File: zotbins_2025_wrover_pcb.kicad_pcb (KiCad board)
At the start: 2 copper layers, 26 parts, among them J1 FFC2B28-24-G, J5 DCJ200-10-A-XX-K_REVA, J6 Conn_01x30_Pin, U1 ESP32-WROVER-E/IE-DEVKIT-C, U2 MCP23017_SP, U3 XC6206P122MR-G, U4 XC6206P282PR-G, U5 LM7805_TO220

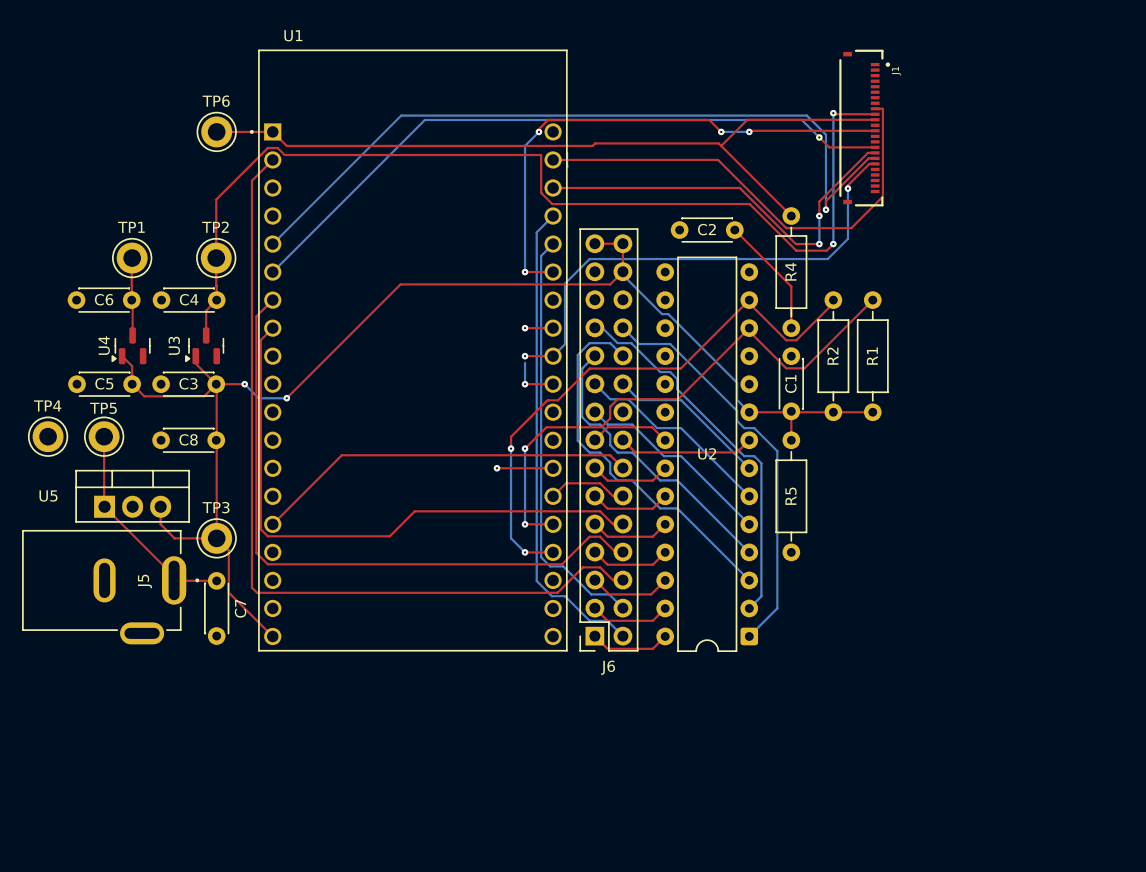
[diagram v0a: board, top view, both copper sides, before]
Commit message: resolved ERC checks, footprint incompatibilities, symbol library not found errors; 3 ERC violations surpressed intentionally
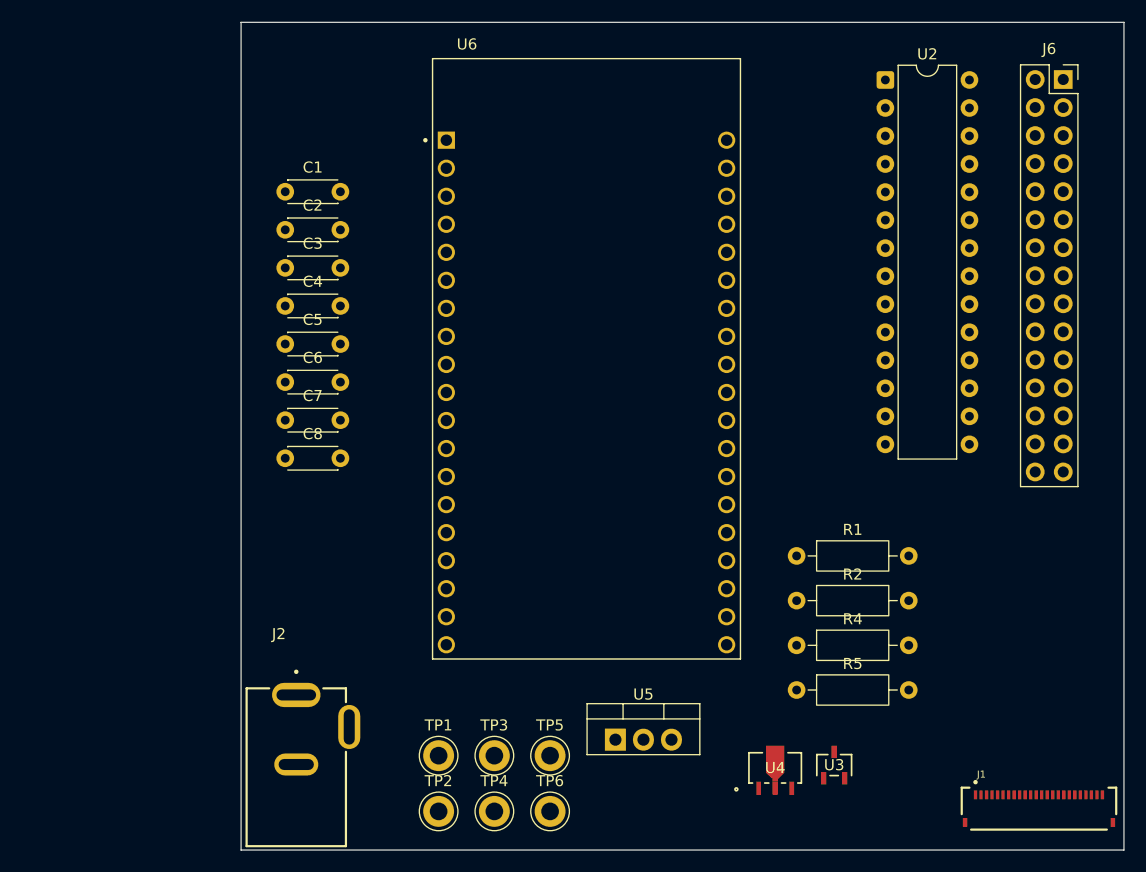
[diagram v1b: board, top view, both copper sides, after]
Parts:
- removed J5: DCJ200-10-A-XX-K_REVA, Connector_BarrelJack:GCT_DCJ200-10-A-XX-K_REVA
- removed U1: ESP32-WROVER-E/IE-DEVKIT-C, MCU_Development_Board:MODULE_ESP32-DEVKITC-32D
- added J2: DCJ200-10-A-XX-K_REVA, Library:GCT_DCJ200-10-A-XX-K_REVA, F.Cu at (105.0, 132.5)
- added U6: ESP32-DEVKITC-32D, ESP32-DEVKITC-32D:MODULE_ESP32-DEVKITC-32D, F.Cu at (131.3, 95.4)
- J1: footprint Connector_FFC-FPC:GCT_FFC2B28-24-G -> Library:GCT_FFC2B28-24-G
- U3: value XC6206P122MR-G -> XC6206P302MR-G; footprint Package_TO_SOT_SMD:SOT-23 -> XC6206P302MR_G:SOT-23_TOR
- U4: footprint Package_TO_SOT_SMD:SOT-23 -> XC6206P282PR_G:SOT-89_TOR
- moved U4 69.7 mm to (148.4, 132.6), turned to 0 degrees
- moved TP6 68.6 mm to (128.0, 136.5)
- moved U3 68.4 mm to (153.7, 132.3), turned to 0 degrees
- moved J6 65.9 mm to (174.5, 70.2), turned to 0 degrees
- moved J1 63.7 mm to (172.3, 136.2), turned to 0 degrees
- moved TP2 54.0 mm to (117.9, 136.5)
- moved TP1 53.0 mm to (117.9, 131.4)
- moved TP4 52.8 mm to (123.0, 136.5)
- moved U2 51.9 mm to (158.4, 70.2), turned to 0 degrees
- moved U5 50.9 mm to (133.9, 130.0)
- moved C1 50.0 mm to (104.0, 80.3), turned to 0 degrees
- moved TP5 49.7 mm to (128.0, 131.4)
- moved C2 40.7 mm to (104.0, 83.8), turned to 0 degrees
- moved R4 38.9 mm to (150.3, 121.5), turned to 0 degrees
- moved TP3 31.9 mm to (123.0, 131.4)
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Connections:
- U3 pad 1: +5V -> GND
- U3 pad 2: GND -> CSI_1V2
- U3 pad 3: CSI_1V2 -> +5V
- U4 pad 1: +5V -> GND
- U4 pad 2: GND -> +5V
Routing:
- net +5V: track 125.1 -> 0.00 mm, vias 2 -> 0
- net CSI_1V2: track 92.4 -> 0.00 mm, vias 2 -> 0
- net /EN: track 74.8 -> 0.00 mm
- net +3V3: track 70.3 -> 0.00 mm
- net /DATA6: track 69.3 -> 0.00 mm, vias 1 -> 0
- net /DATA7: track 61.3 -> 0.00 mm, vias 1 -> 0
- net /GPIO32: track 58.8 -> 0.00 mm
- net /GPIO33: track 53.2 -> 0.00 mm
- net /GPIO_SCK: track 51.2 -> 0.00 mm, vias 2 -> 0
- net /GPIO_SDA: track 50.3 -> 0.00 mm, vias 2 -> 0
- net /XCLK1: track 47.3 -> 0.00 mm, vias 4 -> 0
- net /DATA2: track 45.0 -> 0.00 mm, vias 2 -> 0
- net /TX: track 43.6 -> 0.00 mm
- net /HREF: track 42.3 -> 0.00 mm
- net /PCLK: track 38.3 -> 0.00 mm, vias 2 -> 0
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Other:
- board outline added: 80 x 75 mm

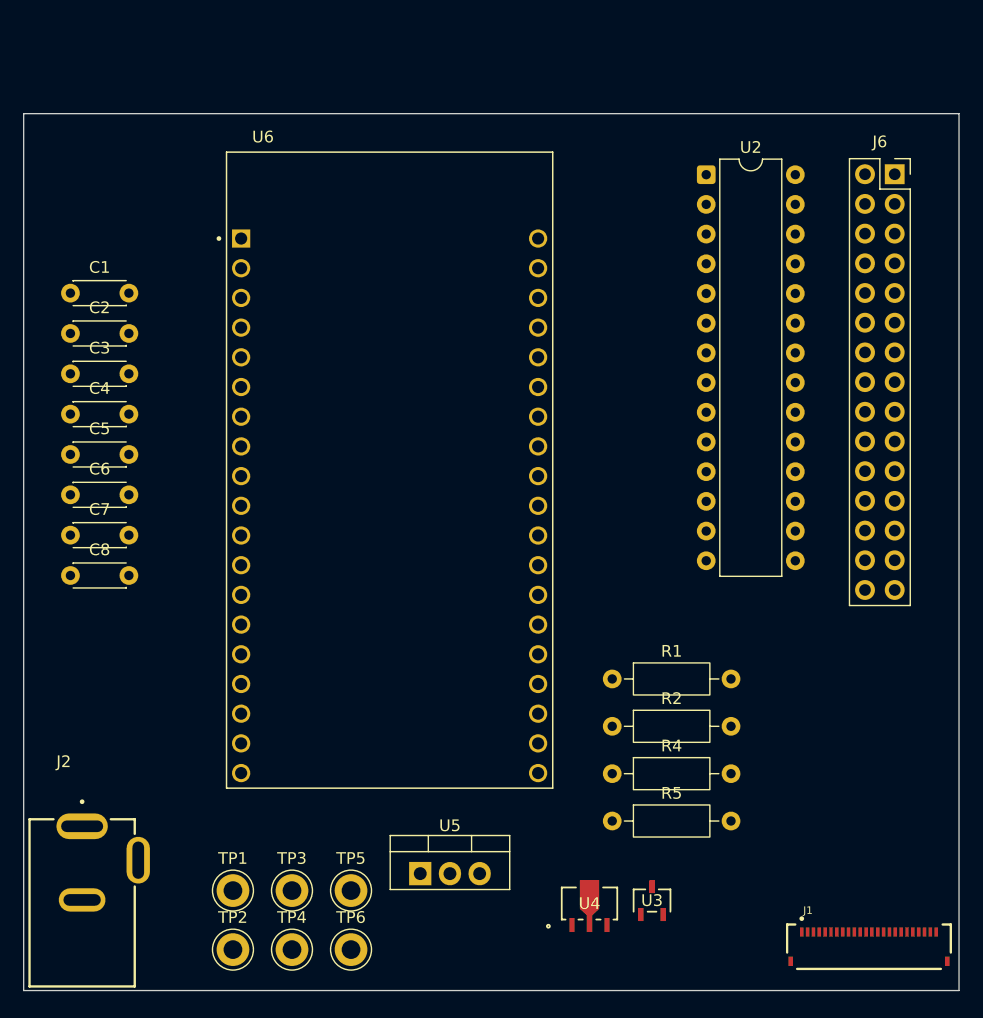
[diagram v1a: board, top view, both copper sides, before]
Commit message: configured power section ratsnest
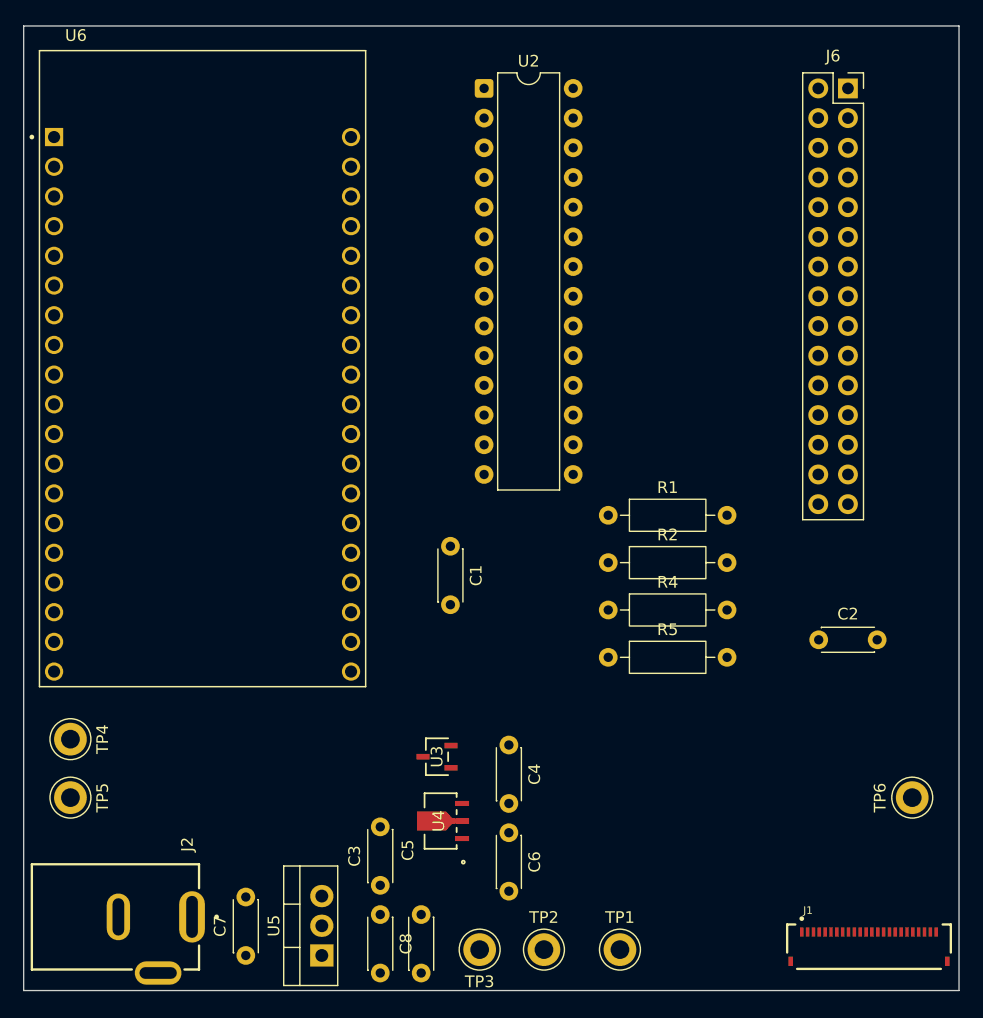
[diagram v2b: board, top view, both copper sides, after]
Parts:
- J2: value DCJ200-10-A-XX-K_REVA -> Barrel Jack
- TP1: value TestPoint -> CSI_2V8
- TP2: value TestPoint -> CSI_1V2
- TP3: value TestPoint -> RegVo
- TP4: value TestPoint -> GND
- TP5: value TestPoint -> Vin
- TP6: value TestPoint -> DOVDD
- moved C2 69.2 mm to (168.0, 110.0)
- moved C3 51.1 mm to (130.5, 131.0), turned to 90 degrees
- moved TP6 49.7 mm to (176.0, 123.5), turned to 90 degrees
- moved C5 49.5 mm to (134.0, 133.5), turned to -90 degrees
- moved C6 47.3 mm to (141.5, 126.5), turned to -90 degrees
- moved C4 47.0 mm to (141.5, 119.0), turned to -90 degrees
- moved C8 39.3 mm to (130.5, 133.5), turned to -90 degrees
- moved C1 39.1 mm to (136.5, 102.0), turned to -90 degrees
- moved C7 39.0 mm to (119.0, 137.0), turned to 90 degrees
- moved TP1 33.5 mm to (151.0, 136.5)
- moved TP2 26.6 mm to (144.5, 136.5)
- moved TP4 26.1 mm to (104.0, 118.5), turned to -90 degrees
- moved TP5 25.3 mm to (104.0, 123.5), turned to -90 degrees
- moved U3 22.1 mm to (135.4, 120.0), turned to 90 degrees
- moved U2 20.4 mm to (139.4, 62.8)
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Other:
- board size 80 x 75 mm -> 80 x 82.5 mm

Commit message: sorted ratsnest
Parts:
- moved R5 24.8 mm to (158.9, 88.4), turned to -90 degrees
- moved R2 23.1 mm to (138.4, 83.4), turned to -90 degrees
- moved R1 22.2 mm to (134.5, 83.4), turned to -90 degrees
- moved R4 22.2 mm to (150.4, 129.7)
- moved TP6 21.8 mm to (158.3, 136.3), turned to 0 degrees
- moved C1 19.6 mm to (142.8, 83.4)
- moved C2 16.5 mm to (160.5, 124.7), turned to 180 degrees
- moved U2 7.50 mm to (146.9, 63.1)
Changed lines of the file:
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@@
 	(footprint "TestPoint:TestPoint_Keystone_5005-5009_Compact"
 		(layer "F.Cu")
-		(at 176 123.5 90)
+		(at 158.35 136.325)
 		(descr "Keystone THM Compact Test Point 5005-5009, http://www.keyelco.com/product-pdf.cfm?p=1314")
 		(tags "Through Hole Mount Test Points")
 		(property "Reference" "TP6"
-			(at 0 -2.75 90)
+			(at 0 -2.75 0)
 			(layer "F.SilkS")
 			(effects
@@
 		)
 		(property "Value" "DOVDD"
-			(at 0 2.75 90)
+			(at 0 2.75 0)
 			(layer "F.Fab")
 			(effects
@@
 		)
 		(property "Datasheet" "~"
-			(at 0 0 90)
+			(at 0 0 0)
 			(unlocked yes)
 			(layer "F.Fab")
@@
 		)
 		(property "Description" "test point"
-			(at 0 0 90)
+			(at 0 0 0)
 			(unlocked yes)
 			(layer "F.Fab")
@@
 		)
 		(fp_text user "${REFERENCE}"
-			(at 0 0 90)
+			(at 0 0 0)
 			(layer "F.Fab")
 			(effects
@@
 		)
 		(pad "1" thru_hole circle
-			(at 0 0 90)
+			(at 0 0)
 			(size 2.8 2.8)
 			(drill 1.6)
@@
 	(footprint "Capacitor_THT:C_Disc_D4.3mm_W1.9mm_P5.00mm"
 		(layer "F.Cu")
-		(at 136.5 102 -90)
+		(at 142.775 83.4 -90)
 		(descr "C, Disc series, Radial, pin pitch=5.00mm, diameter*width=4.3*1.9mm^2, Capacitor, http://www.vishay.com/docs/45233/krseries.pdf")
 		(tags "C Disc series Radial pin pitch 5.00mm diameter 4.3mm width 1.9mm Capacitor")
@@
 	(footprint "Resistor_THT:R_Axial_DIN0207_L6.3mm_D2.5mm_P10.16mm_Horizontal"
 		(layer "F.Cu")
-		(at 150 99.35)
+		(at 134.5 83.415 -90)
 		(descr "Resistor, Axial_DIN0207 series, Axial, Horizontal, pin pitch=10.16mm, 0.25W = 1/4W, length*diameter=6.3*2.5mm^2, http://cdn-reichelt.de/documents/datenblatt/B400/1_4W%23YAG.pdf")
 		(tags "Resistor Axial_DIN0207 series Axial Horizontal pin pitch 10.16mm 0.25W = 1/4W length 6.3mm diameter 2.5mm")
 		(property "Reference" "R1"
-			(at 5.08 -2.37 0)
+			(at 5.08 -2.37 90)
 			(layer "F.SilkS")
 			(effects
@@
 		)
 		(property "Value" "10k"
-			(at 5.08 2.37 0)
+			(at 5.08 2.37 90)
 			(layer "F.Fab")
 			(effects
@@
 		)
 		(property "Datasheet" "~"
-			(at 0 0 0)
+			(at 0 0 90)
 			(layer "F.Fab")
 			(hide yes)
@@
 		)
 		(property "Description" "Resistor, small symbol"
-			(at 0 0 0)
+			(at 0 0 90)
 			(layer "F.Fab")
 			(hide yes)
@@
 		)
 		(fp_text user "${REFERENCE}"
-			(at 5.08 0 0)
+			(at 5.08 0 90)
 			(layer "F.Fab")
 			(effects
@@
 		)
 		(pad "1" thru_hole circle
-			(at 0 0)
+			(at 0 0 270)
 			(size 1.6 1.6)
 			(drill 0.8)
@@
 		)
 		(pad "2" thru_hole circle
-			(at 10.16 0)
+			(at 10.16 0 270)
 			(size 1.6 1.6)
 			(drill 0.8)
@@
 	(footprint "Capacitor_THT:C_Disc_D4.3mm_W1.9mm_P5.00mm"
 		(layer "F.Cu")
-		(at 168 110)
+		(at 160.475 124.725 180)
 		(descr "C, Disc series, Radial, pin pitch=5.00mm, diameter*width=4.3*1.9mm^2, Capacitor, http://www.vishay.com/docs/45233/krseries.pdf")
 		(tags "C Disc series Radial pin pitch 5.00mm diameter 4.3mm width 1.9mm Capacitor")
@@
 		(attr through_hole)
 		(fp_line
-			(start 0.23 -1.07)
-			(end 4.77 -1.07)
+			(start 4.77 1.07)
+			(end 0.23 1.07)
 			(stroke
 				(width 0.12)
@@
 		)
 		(fp_line
-			(start 0.23 -1.014)
-			(end 0.23 -1.07)
+			(start 4.77 1.014)
+			(end 4.77 1.07)
 			(stroke
 				(width 0.12)
@@
 		)
 		(fp_line
-			(start 4.77 1.014)
-			(end 4.77 1.07)
+			(start 0.23 -1.014)
+			(end 0.23 -1.07)
 			(stroke
 				(width 0.12)
@@
 		)
 		(fp_line
-			(start 4.77 1.07)
-			(end 0.23 1.07)
+			(start 0.23 -1.07)
+			(end 4.77 -1.07)
 			(stroke
 				(width 0.12)
@@
 		)
 		(pad "1" thru_hole circle
-			(at 0 0)
+			(at 0 0 180)
 			(size 1.6 1.6)
 			(drill 0.8)
@@
 		)
 		(pad "2" thru_hole circle
-			(at 5 0)
+			(at 5 0 180)
 			(size 1.6 1.6)
 			(drill 0.8)
@@
 	(footprint "Package_DIP:DIP-28_W7.62mm"
 		(layer "F.Cu")
-		(at 139.38 62.84)
+		(at 146.88 63.06)
 		(descr "28-lead though-hole mounted DIP package, row spacing 7.62mm (300 mils)")
 		(tags "THT DIP DIL PDIP 2.54mm 7.62mm 300mil")
@@
 	(footprint "Resistor_THT:R_Axial_DIN0207_L6.3mm_D2.5mm_P10.16mm_Horizontal"
 		(layer "F.Cu")
-		(at 150 107.45)
+		(at 150.365 129.675)
 		(descr "Resistor, Axial_DIN0207 series, Axial, Horizontal, pin pitch=10.16mm, 0.25W = 1/4W, length*diameter=6.3*2.5mm^2, http://cdn-reichelt.de/documents/datenblatt/B400/1_4W%23YAG.pdf")
 		(tags "Resistor Axial_DIN0207 series Axial Horizontal pin pitch 10.16mm 0.25W = 1/4W length 6.3mm diameter 2.5mm")
@@
 	(footprint "Resistor_THT:R_Axial_DIN0207_L6.3mm_D2.5mm_P10.16mm_Horizontal"
 		(layer "F.Cu")
-		(at 150 111.5)
+		(at 158.925 88.415 -90)
 		(descr "Resistor, Axial_DIN0207 series, Axial, Horizontal, pin pitch=10.16mm, 0.25W = 1/4W, length*diameter=6.3*2.5mm^2, http://cdn-reichelt.de/documents/datenblatt/B400/1_4W%23YAG.pdf")
 		(tags "Resistor Axial_DIN0207 series Axial Horizontal pin pitch 10.16mm 0.25W = 1/4W length 6.3mm diameter 2.5mm")
 		(property "Reference" "R5"
-			(at 5.08 -2.37 0)
+			(at 5.08 -2.37 90)
 			(layer "F.SilkS")
 			(effects
@@
 		)
 		(property "Value" "10k"
-			(at 5.08 2.37 0)
+			(at 5.08 2.37 90)
 			(layer "F.Fab")
 			(effects
@@
 		)
 		(property "Datasheet" "~"
-			(at 0 0 0)
+			(at 0 0 90)
 			(layer "F.Fab")
 			(hide yes)
@@
 		)
 		(property "Description" "Resistor, small symbol"
-			(at 0 0 0)
+			(at 0 0 90)
 			(layer "F.Fab")
 			(hide yes)
@@
 		)
 		(fp_text user "${REFERENCE}"
-			(at 5.08 0 0)
+			(at 5.08 0 90)
 			(layer "F.Fab")
 			(effects
@@
 		)
 		(pad "1" thru_hole circle
-			(at 0 0)
+			(at 0 0 270)
 			(size 1.6 1.6)
 			(drill 0.8)
@@
 		)
 		(pad "2" thru_hole circle
-			(at 10.16 0)
+			(at 10.16 0 270)
 			(size 1.6 1.6)
 			(drill 0.8)
@@
 	(footprint "Resistor_THT:R_Axial_DIN0207_L6.3mm_D2.5mm_P10.16mm_Horizontal"
 		(layer "F.Cu")
-		(at 150 103.4)
+		(at 138.4 83.415 -90)
 		(descr "Resistor, Axial_DIN0207 series, Axial, Horizontal, pin pitch=10.16mm, 0.25W = 1/4W, length*diameter=6.3*2.5mm^2, http://cdn-reichelt.de/documents/datenblatt/B400/1_4W%23YAG.pdf")
 		(tags "Resistor Axial_DIN0207 series Axial Horizontal pin pitch 10.16mm 0.25W = 1/4W length 6.3mm diameter 2.5mm")
 		(property "Reference" "R2"
-			(at 5.08 -2.37 0)
+			(at 5.08 -2.37 90)
 			(layer "F.SilkS")
 			(effects
@@
 		)
 		(property "Value" "10k"
-			(at 5.08 2.37 0)
+			(at 5.08 2.37 90)
 			(layer "F.Fab")
 			(effects
@@
 		)
 		(property "Datasheet" "~"
-			(at 0 0 0)
+			(at 0 0 90)
 			(layer "F.Fab")
 			(hide yes)
@@
 		)
 		(property "Description" "Resistor, small symbol"
-			(at 0 0 0)
+			(at 0 0 90)
 			(layer "F.Fab")
 			(hide yes)
@@
 		)
 		(fp_text user "${REFERENCE}"
-			(at 5.08 0 0)
+			(at 5.08 0 90)
 			(layer "F.Fab")
 			(effects
@@
 		)
 		(pad "1" thru_hole circle
-			(at 0 0)
+			(at 0 0 270)
 			(size 1.6 1.6)
 			(drill 0.8)
@@
 		)
 		(pad "2" thru_hole circle
-			(at 10.16 0)
+			(at 10.16 0 270)
 			(size 1.6 1.6)
 			(drill 0.8)
